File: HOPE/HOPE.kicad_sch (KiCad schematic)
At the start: 8 parts

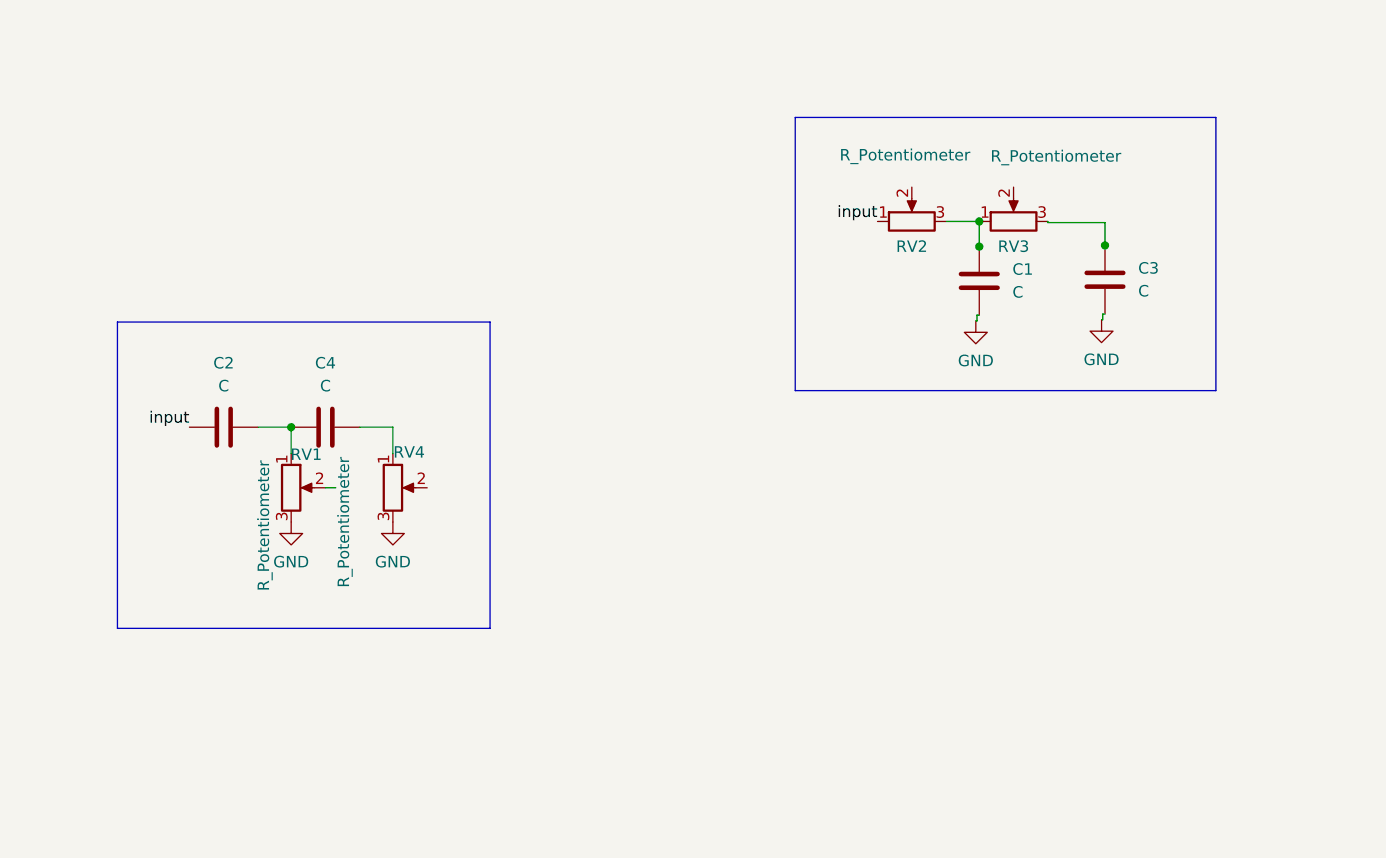
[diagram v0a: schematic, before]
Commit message: commit edits to add buffer to filter
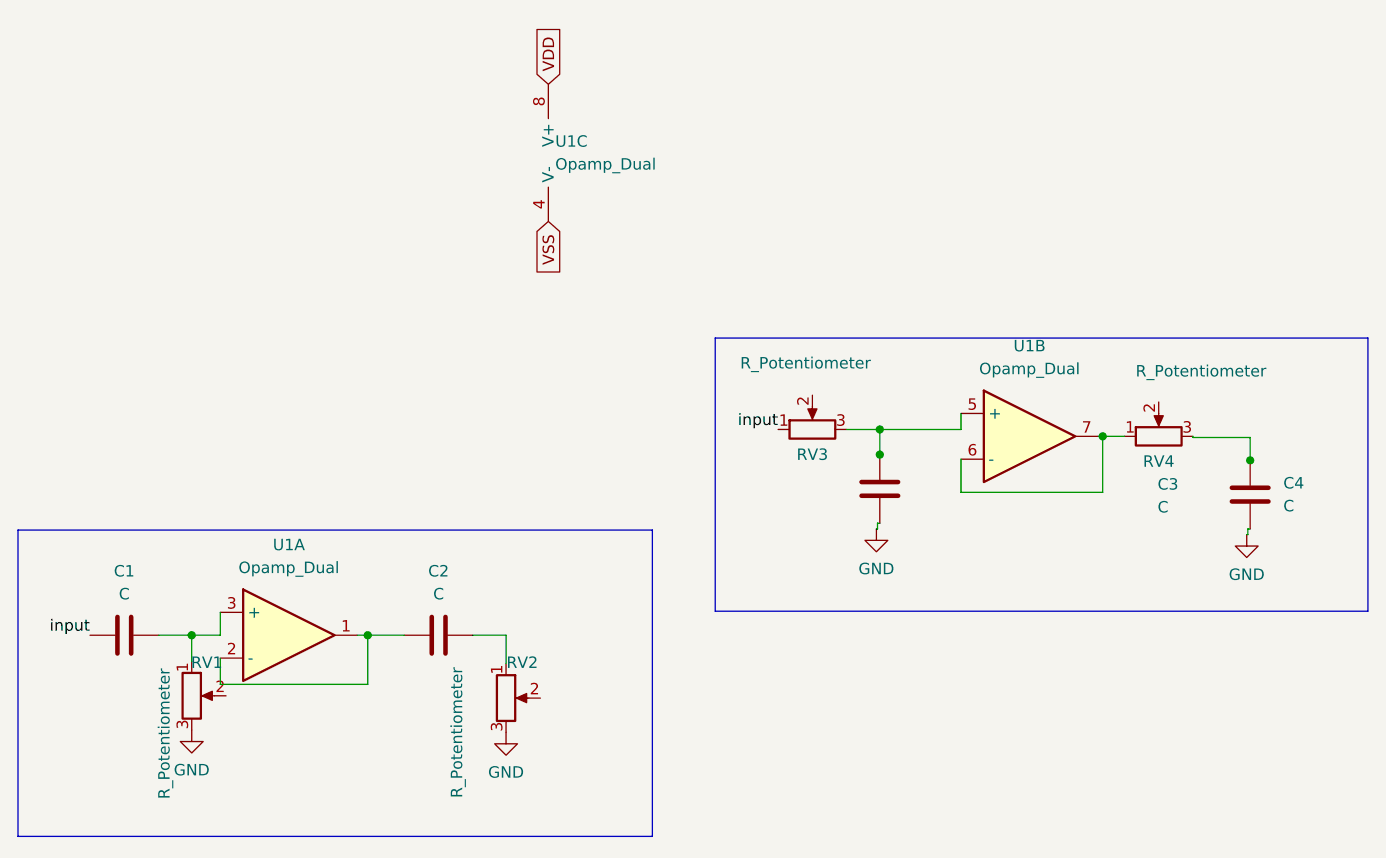
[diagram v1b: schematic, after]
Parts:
- added U1: Opamp_Dual, symbol Device:Opamp_Dual
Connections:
- net GND: now also C4.2, RV2.3; no longer C1.2, RV4.3
- net input: now also C1.1, RV3.1; no longer C2.1, RV2.1
- net at RV4.1: now also U1.6 (-), U1.7; no longer C4.2
- net at C3.1, RV3.3: now also U1.5 (+)
- new net: C2.1, U1.1, U1.2 (-)
- new net: C1.2, RV1.1, U1.3 (+)
- new net: C4.1, RV4.3
- new net: C2.2, RV2.1
- new net VDD: U1.8 (V+)
- new net VSS: U1.4 (V-)
